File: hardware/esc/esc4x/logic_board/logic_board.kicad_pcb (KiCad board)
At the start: 4 copper layers, 18.3 x 28.1 mm, 112 parts, among them J1 Conn_01x11, J2 Conn_01x03, J3 Conn_01x06, J4 Conn_01x11, J5 Conn_01x02, J6 Conn_01x02, J7 Conn_01x06, J8 Conn_01x03, U1 STM32F051K8Ux, U2 DRV8300DRGE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

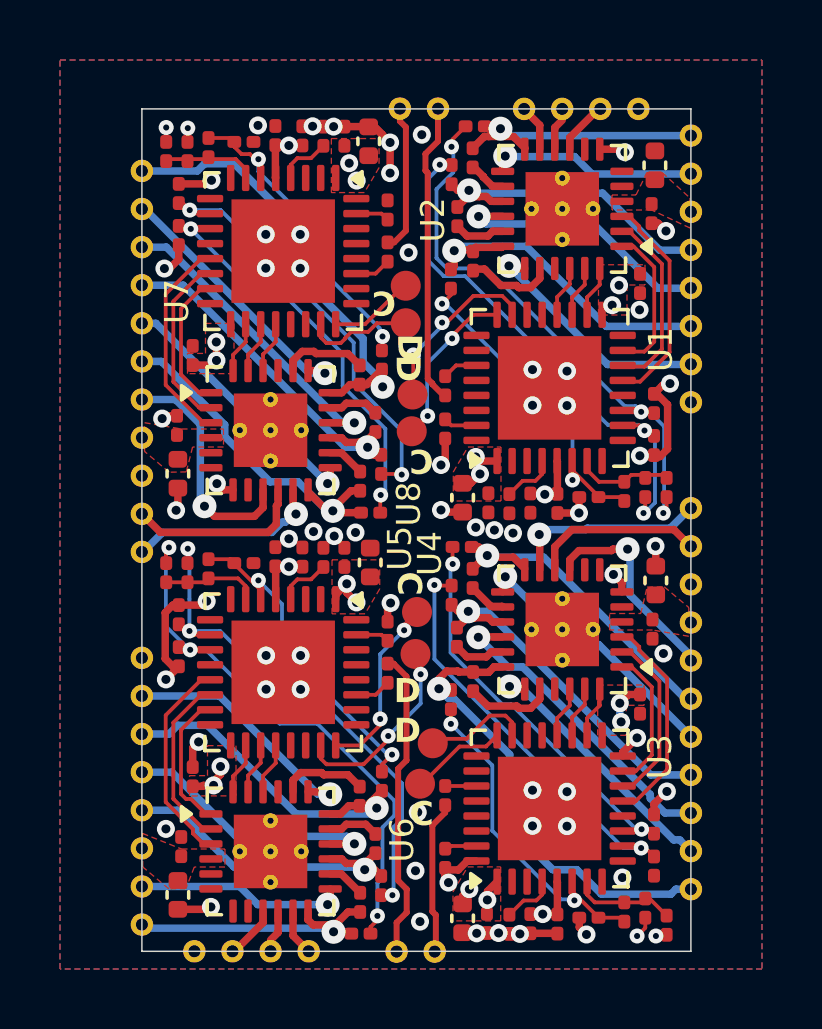
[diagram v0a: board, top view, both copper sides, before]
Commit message: thermal vias fix
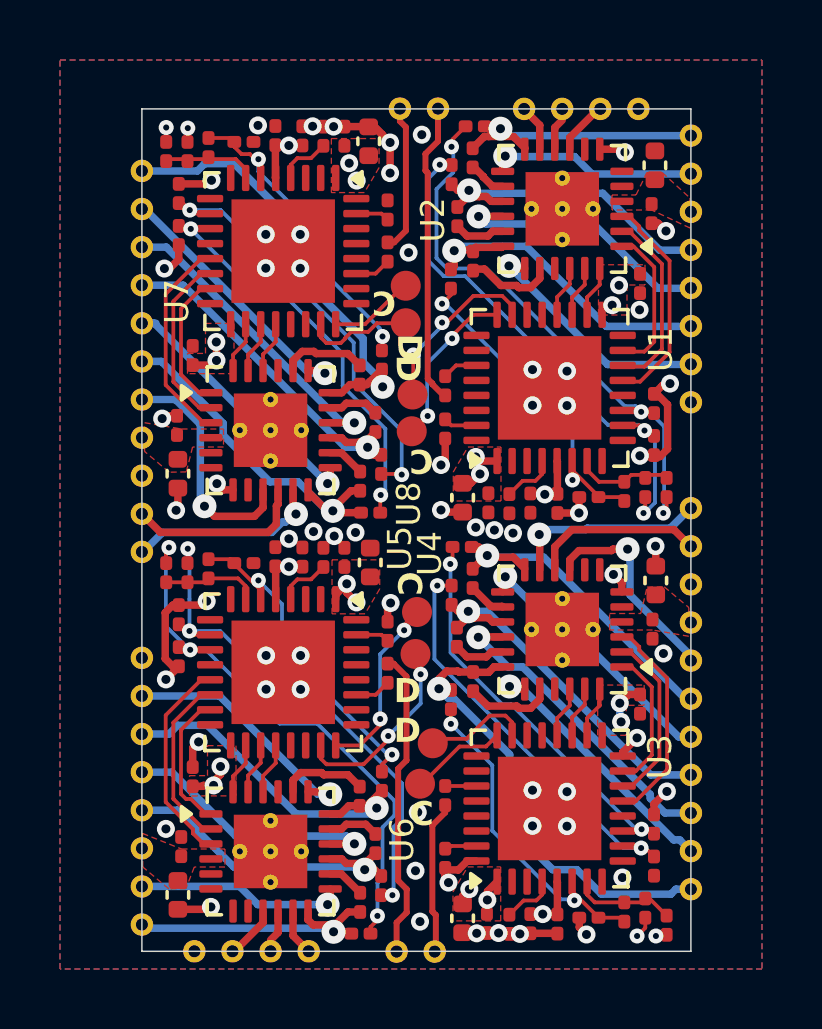
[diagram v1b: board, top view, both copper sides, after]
